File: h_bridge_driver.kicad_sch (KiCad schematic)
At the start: 66 parts, among them IC1 DRV8702QRHBRQ1, J1 IN1, J2 IN2, J3 SUPP, J4 IN1, J5 IN1, J6 GND, Q1 SUD80460E, Q2 SUD80460E, Q3 SUD80460E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

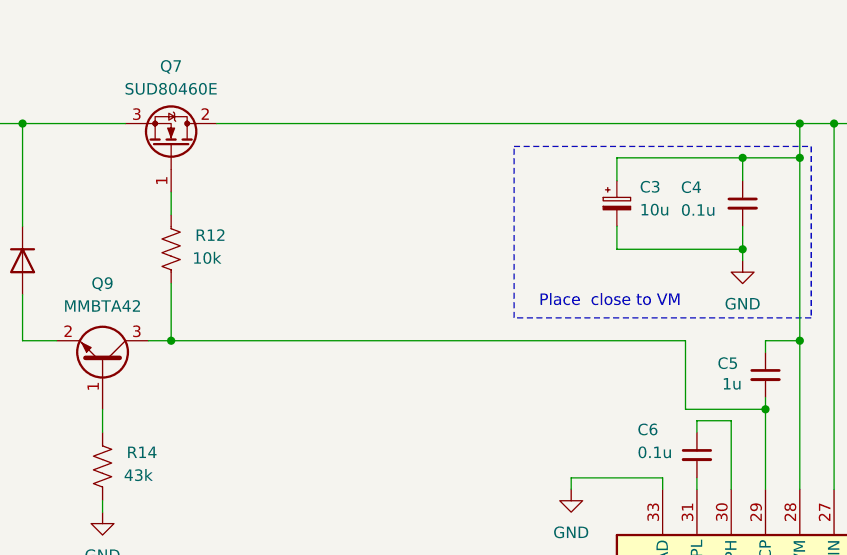
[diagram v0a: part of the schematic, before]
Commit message: Fixed incorrect plane dimensions on power layer. Fixed wrong connection of BJT to RVP MOSFET gate.
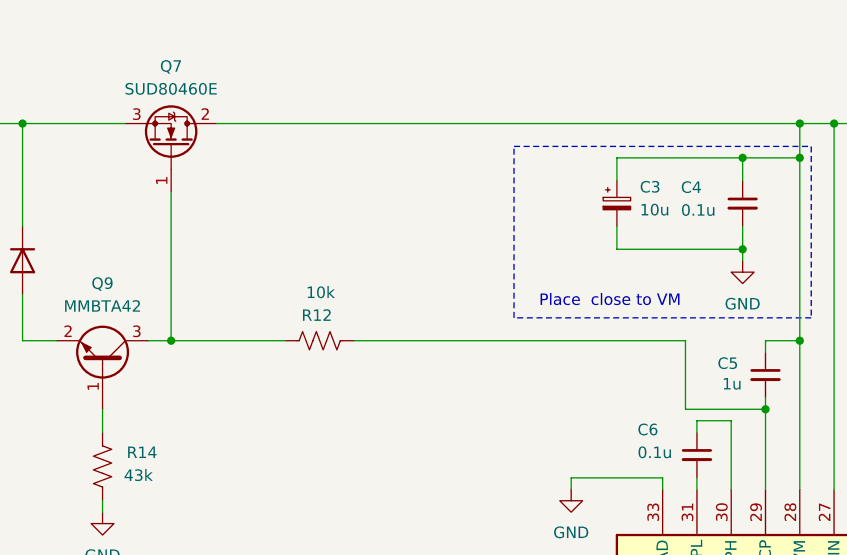
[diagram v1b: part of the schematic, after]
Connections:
- net at C5.2, IC1.29 (VCP), R12.1: no longer Q9.3 (C)
- net at Q7.1 (G), R12.2: now also Q9.3 (C)
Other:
- moved on the sheet: R12
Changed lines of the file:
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@@
 	(title_block
 		(title "H-Bridge Driver Board")
-		(date "2025-03-13")
-		(rev "v0.1")
+		(date "2025-03-30")
+		(rev "v0.2")
 	)
 	(junction
@@
 	)
 	(junction
-		(at 252.73 123.19)
+		(at 77.47 82.55)
 		(diameter 0)
 		(color 0 0 0 0)
 	)
 	(junction
-		(at 297.18 210.82)
+		(at 252.73 123.19)
 		(diameter 0)
 		(color 0 0 0 0)
 	)
 	(junction
-		(at 77.47 82.55)
+		(at 297.18 210.82)
 		(diameter 0)
 		(color 0 0 0 0)
@@
 	(wire
 		(pts
-			(xy 134.62 82.55) (xy 77.47 82.55)
+			(xy 134.62 82.55) (xy 97.79 82.55)
 		)
 		(stroke
@@
 	(wire
 		(pts
-			(xy 74.93 82.55) (xy 77.47 82.55)
-		)
-		(stroke
-			(width 0)
-			(type default)
-		)
-	)
-	(wire
-		(pts
 			(xy 382.27 134.62) (xy 382.27 138.43)
 		)
@@
 	(wire
 		(pts
-			(xy 77.47 82.55) (xy 77.47 76.2)
+			(xy 151.13 160.02) (xy 151.13 180.34)
 		)
 		(stroke
@@
 	(wire
 		(pts
-			(xy 151.13 160.02) (xy 151.13 180.34)
+			(xy 143.51 204.47) (xy 143.51 205.74)
 		)
 		(stroke
@@
 	(wire
 		(pts
-			(xy 143.51 204.47) (xy 143.51 205.74)
+			(xy 320.04 96.52) (xy 349.25 96.52)
 		)
 		(stroke
@@
 	(wire
 		(pts
-			(xy 320.04 96.52) (xy 349.25 96.52)
+			(xy 77.47 82.55) (xy 90.17 82.55)
 		)
 		(stroke
@@
 	(wire
 		(pts
+			(xy 77.47 66.04) (xy 77.47 82.55)
+		)
+		(stroke
+			(width 0)
+			(type default)
+		)
+	)
+	(wire
+		(pts
 			(xy 171.45 180.34) (xy 176.53 180.34)
 		)
@@
 	(wire
 		(pts
-			(xy 105.41 153.67) (xy 105.41 156.21)
+			(xy 74.93 82.55) (xy 77.47 82.55)
 		)
 		(stroke
@@
 	(wire
 		(pts
-			(xy 151.13 58.42) (xy 151.13 99.06)
+			(xy 105.41 153.67) (xy 105.41 156.21)
 		)
 		(stroke
@@
 	(wire
 		(pts
-			(xy 102.87 118.11) (xy 102.87 111.76)
+			(xy 151.13 58.42) (xy 151.13 99.06)
 		)
 		(stroke
@@
 	(wire
 		(pts
-			(xy 213.36 116.84) (xy 220.98 116.84)
+			(xy 102.87 118.11) (xy 102.87 111.76)
 		)
 		(stroke
@@
 	(wire
 		(pts
-			(xy 177.8 148.59) (xy 177.8 144.78)
+			(xy 213.36 116.84) (xy 220.98 116.84)
 		)
 		(stroke
@@
 	(wire
 		(pts
-			(xy 77.47 66.04) (xy 77.47 68.58)
+			(xy 177.8 148.59) (xy 177.8 144.78)
 		)
 		(stroke
@@
 	(symbol
 		(lib_id "Device:R_US")
-		(at 77.47 72.39 180)
+		(at 93.98 82.55 270)
 		(unit 1)
 		(exclude_from_sim no)
@@
 		(dnp no)
 		(property "Reference" "R12"
-			(at 83.566 70.866 0)
+			(at 91.948 79.756 90)
 			(effects
 				(font
@@
 		)
 		(property "Value" "10k"
-			(at 83.058 73.406 0)
+			(at 92.456 77.216 90)
 			(effects
 				(font
@@
 		)
 		(property "Footprint" "Resistor_SMD:R_0805_2012Metric_Pad1.20x1.40mm_HandSolder"
-			(at 76.454 72.136 90)
+			(at 93.726 83.566 90)
 			(effects
 				(font
@@
 		)
 		(property "Datasheet" "~"
-			(at 77.47 72.39 0)
+			(at 93.98 82.55 0)
 			(effects
 				(font
@@
 		)
 		(property "Description" "Resistor, US symbol"
-			(at 77.47 72.39 0)
+			(at 93.98 82.55 0)
 			(effects
 				(font
